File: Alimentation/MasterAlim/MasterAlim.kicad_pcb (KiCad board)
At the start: 4 copper layers, 85 x 42.8 mm, 53 parts, among them J1 Ext-Con, J10 Reg Log, J11 AU Logic, J12 INHIBIT, J13 ToRegul, J2 Alim logique, J3 Batt IN, J4 INHIBIT, J5 ToRegul, J6 INHIBIT, J7 ToRegul, J8 INHIBIT, J9 ToRegul, U1 74LVC1G02, U2 74LVC1G02, U3 74LVC1G02, U4 74LVC1G02, U8 PCF8574A

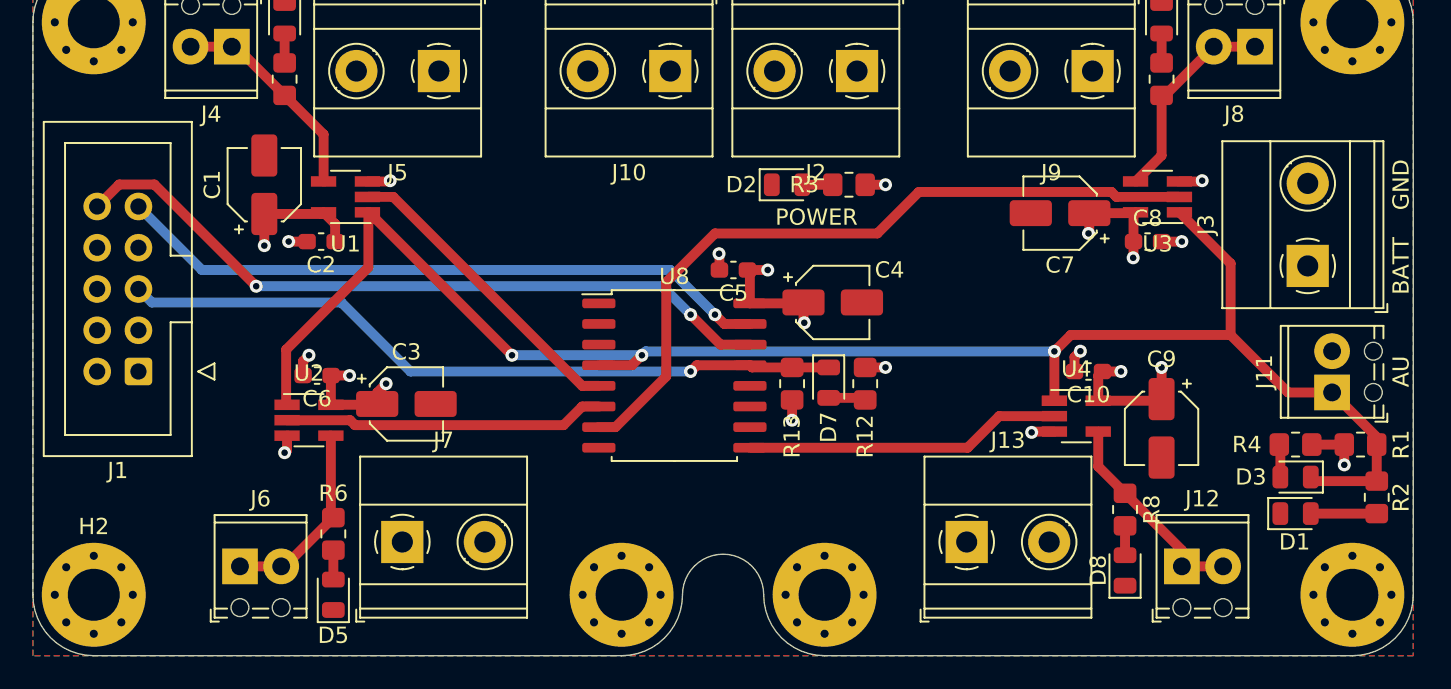
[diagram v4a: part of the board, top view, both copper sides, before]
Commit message: Finalisation routage master alim
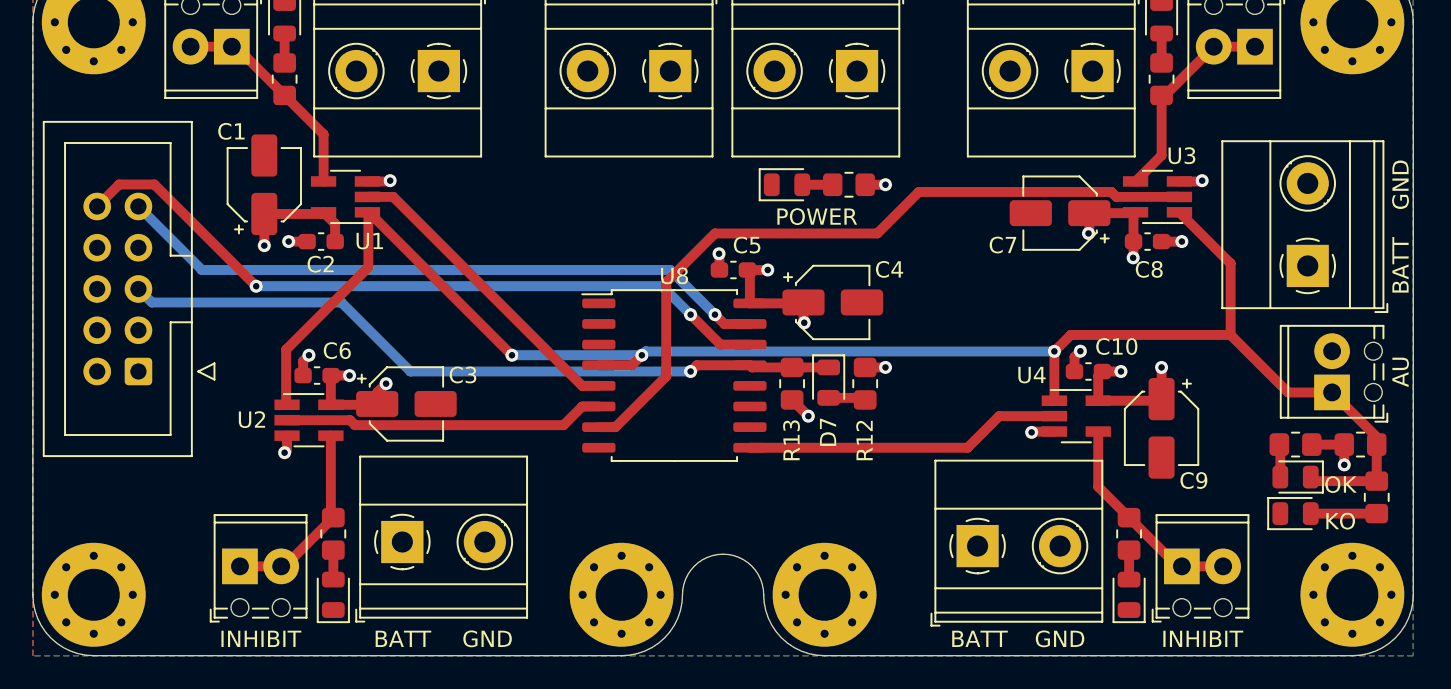
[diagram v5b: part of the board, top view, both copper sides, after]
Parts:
- moved D8 1.52 mm to (167.5, 89.0)
- moved R8 1.52 mm to (167.5, 85.2)
- moved J13 0.72 mm to (158.2, 86.0)
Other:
- board text added: "KO"
- board text added: "OK"

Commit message: Rework suite point robot
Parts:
- removed H6, H7, H8: MountingHole_Pad, MountingHole:MountingHole_3.2mm_M3_Pad_Via
- added H3: MountingHole_Pad, MountingHole:MountingHole_3.2mm_M3_Pad_Via, F.Cu at (164.0, 48.0)
- moved J2 29.9 mm to (129.2, 77.5), turned to 0 degrees
- moved H4 29.1 mm to (164.0, 80.2)
- moved R1 27.1 mm to (158.0, 66.8), turned to 270 degrees
- moved R12 25.4 mm to (127.3, 67.5), turned to 0 degrees
- moved C4 23.9 mm to (127.8, 60.5), turned to 270 degrees
- moved D8 23.4 mm to (154.8, 69.4), turned to 270 degrees
- moved J8 22.8 mm to (153.3, 49.2)
- moved C9 22.4 mm to (150.2, 67.2), turned to 180 degrees
- moved R13 22.1 mm to (127.3, 65.5), turned to 0 degrees
- moved J12 21.6 mm to (150.8, 79.0)
- moved R2 21.6 mm to (164.8, 71.0), turned to 180 degrees
- moved D1 21.2 mm to (161.0, 71.0)
- moved R3 21.1 mm to (130.2, 70.5), turned to 0 degrees
- moved D7 21.0 mm to (130.2, 66.5)
- moved J9 20.6 mm to (145.5, 50.8)
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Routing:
- net GND: track 11.6 -> 37.5 mm, vias 9 -> 5
- net /PIL_T3: track 45.3 -> 20.4 mm, vias 0 -> 2
- net /AU: track 104.6 -> 86.6 mm, vias 3 -> 4
- net SDA: track 40.6 -> 28.8 mm
- net /IRQ: track 44.8 -> 33.5 mm, vias 1 -> 0
- net SCL: track 44.8 -> 33.6 mm, vias 2 -> 1
- net /PIL_T2: track 19.8 -> 25.3 mm, vias 0 -> 2
- net /PilAlim1/Y: track 13.3 -> 16.7 mm
- net /sheet602E5F6A/Y: track 13.1 -> 10.1 mm
- net Net-(D1-Pad2): track 4.06 -> 1.81 mm
- net +5V: track 46.1 -> 43.8 mm, vias 13 -> 9
- net /sheet602E5506/Y: track 12.1 -> 14.0 mm
- net /PIL_T1: track 19.1 -> 19.9 mm, vias 0 -> 2
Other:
- board size 85 x 42.8 mm -> 67 x 39.8 mm
- board text added: "1"
- board text added: "2"
- board text added: "3"
- board text added: "4"
- board text added: "L"
- board text removed: "POWER"

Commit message: Finalisation alimentations
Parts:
- removed C4, C7, C9: 1u, Capacitor_SMD:CP_Elec_4x5.3
- removed H4: MountingHole_Pad, MountingHole:MountingHole_3.2mm_M3_Pad_Via
- removed J10: Reg Log, TerminalBlock_Phoenix:TerminalBlock_Phoenix_MKDS-1,5-2-5.08_1x02_P5.08mm_Horizontal
- removed J13, J5, J7, J9: ToRegul, TerminalBlock_Phoenix:TerminalBlock_Phoenix_MKDS-1,5-2-5.08_1x02_P5.08mm_Horizontal
- removed J3: Batt IN, TerminalBlock_Phoenix:TerminalBlock_Phoenix_MKDS-1,5-2-5.08_1x02_P5.08mm_Horizontal
- moved R8 59.6 mm to (104.8, 40.8)
- moved D8 59.6 mm to (104.8, 37.0)
- moved J12 55.9 mm to (110.5, 40.2), turned to 180 degrees
- moved C10 51.3 mm to (106.8, 45.8), turned to 90 degrees
- moved U4 49.6 mm to (110.0, 45.8), turned to 180 degrees
- moved D6 46.2 mm to (113.8, 37.0), turned to 270 degrees
- moved R7 43.2 mm to (113.8, 40.8), turned to 90 degrees
- moved J6 42.8 mm to (128.5, 40.2), turned to 180 degrees
- moved J11 41.5 mm to (121.5, 66.5), turned to 0 degrees
- moved D3 38.5 mm to (127.2, 65.5), turned to 90 degrees
- moved C8 36.9 mm to (115.8, 45.8), turned to 90 degrees
- moved R2 36.6 mm to (128.2, 68.2), turned to 0 degrees
- moved J8 35.0 mm to (119.5, 40.2)
- moved R4 34.8 mm to (128.2, 62.8), turned to 180 degrees
- moved D5 33.7 mm to (122.8, 37.0)
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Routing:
- net +5V: track 43.8 -> 62.2 mm, vias 9 -> 11
- net /PIL_T2: track 25.3 -> 9.37 mm
- net GND: track 37.5 -> 49.7 mm, vias 5 -> 10
- net /PIL_T3: track 20.4 -> 9.09 mm, vias 2 -> 0
- net /PIL_T4: track 19.1 -> 8.27 mm, vias 0 -> 2
- net SCL: track 33.6 -> 22.9 mm
- net /AU: track 86.6 -> 96.6 mm, vias 4 -> 3
- net SDA: track 28.8 -> 19.8 mm
- net /PIL_T1: track 19.9 -> 13.5 mm
- net /PilAlim1/Y: track 16.7 -> 11.2 mm
- net /sheet602E5506/Y: track 14.0 -> 11.2 mm
- net /sheet602E5F64/Y: track 13.0 -> 11.2 mm
- net /IRQ: track 33.5 -> 32.3 mm, vias 0 -> 2
- net /sheet602E5F6A/Y: track 10.1 -> 11.2 mm
- added copper zone on In2.Cu, net +5V
- removed copper zone on In1.Cu, net +5V
- removed copper zone on In2.Cu, net +BATT
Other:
- board size 67 x 39.8 mm -> 46.5 x 36.2 mm
- board text added: "MOD.1"
- board text added: "MOD.2"
- board text added: "MOD.3"
- board text added: "MOD.4"
- board text removed: "1"
- board text removed: "2"
- board text removed: "3"
- board text removed: "4"
- board text removed: "BATT"
- board text removed: "INHIBIT"
- board text removed: "KO"
- board text removed: "L"
- board text removed: "OK"

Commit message: Finalisation pour commande pack Alimentation 14/02/2021
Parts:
- C1, C3: footprint Capacitor_SMD:CP_Elec_4x5.3 -> Capacitor_THT:CP_Radial_D5.0mm_P2.50mm
- moved G*** 1.46 mm to (122.2, 56.2)
- moved C3 1.25 mm to (113.8, 49.5)
- moved C1 0.56 mm to (132.0, 50.2)
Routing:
- net /AU: track 96.6 -> 82.3 mm, vias 3 -> 4
- net +5V: track 62.2 -> 48.7 mm, vias 11 -> 6
- net /IRQ: track 32.3 -> 34.1 mm
- net GND: track 49.7 -> 47.9 mm, vias 10 -> 8
- net /PIL_T1: track 13.5 -> 15.2 mm, vias 2 -> 0
- net SCL: track 22.9 -> 22.8 mm, vias 1 -> 0
- net SDA: track 19.8 -> 19.7 mm, vias 1 -> 0
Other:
- board text added: "JLCJLCJLCJLC"
